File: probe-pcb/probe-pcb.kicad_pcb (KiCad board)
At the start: 2 copper layers, 38.8 x 48.2 mm, 36 parts, among them J1 IDC_HEADER_02x08, J2 IDC_HEADER_2x12, U1 SN74AXC8T245, U2 DS90LV047A, U3 MIC5205-3.3YM5, U4 DS90LV047A

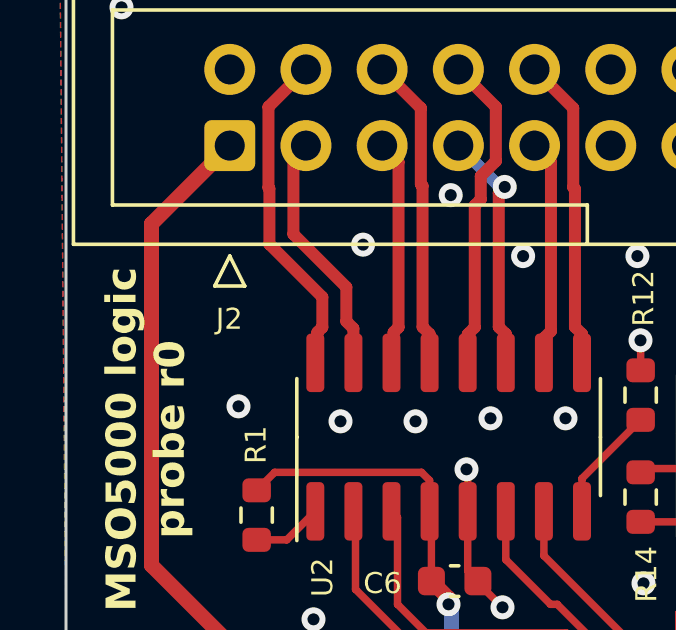
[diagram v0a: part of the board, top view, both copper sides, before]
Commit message: Add 3d model for 2x12 pin header (missing in kicad library), add readme
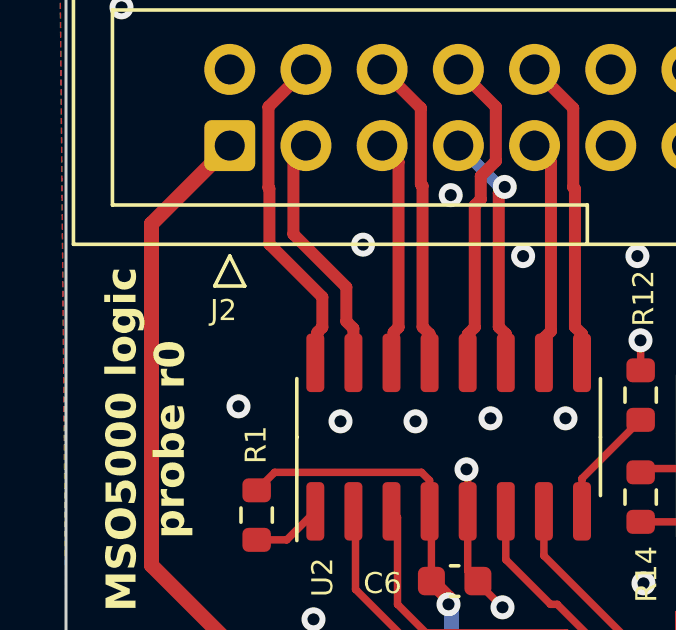
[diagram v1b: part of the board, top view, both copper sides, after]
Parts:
- J2: footprint Connector_IDC:IDC-Header_2x12_P2.54mm_Vertical -> idc:IDC-Header_2x12_P2.54mm_Vertical
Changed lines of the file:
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@@
     )
   )
-  (footprint "Connector_IDC:IDC-Header_2x12_P2.54mm_Vertical" (layer "F.Cu")
+  (footprint "idc:IDC-Header_2x12_P2.54mm_Vertical" (layer "F.Cu")
     (at 99.458 60.259 90)
     (descr "Through hole IDC box header, 2x12, 2.54mm pitch, DIN 41651 / IEC 60603-13, double rows, https://docs.google.com/spreadsheets/d/16SsEcesNF15N3Lb4niX7dcUr-NY5_MFPQhobNuNppn4/edit#gid=0")
@@
     (property "ki_keywords" "connector")
     (attr through_hole)
-    (fp_text reference "J2" (at -5.781 -0.017 180) (layer "F.SilkS")
+    (fp_text reference "J2" (at -5.491 -0.208) (layer "F.SilkS")
         (effects (font (size 0.7 0.7) (thickness 0.15)))
     )
@@
         (effects (font (size 1 1) (thickness 0.15)))
     )
-    (fp_text user "${REFERENCE}" (at 1.27 13.97) (layer "F.Fab")
+    (fp_text user "${REFERENCE}" (at 1.27 13.97 180) (layer "F.Fab")
         (effects (font (size 1 1) (thickness 0.15)))
     )
@@
     (pad "24" thru_hole circle (at 2.54 27.94 90) (size 1.7 1.7) (drill 1) (layers "*.Cu" "*.Mask")
       (net 2 "GND") (pinfunction "Pin_24") (pintype "passive"))
-    (model "${KICAD6_3DMODEL_DIR}/Connector_IDC.3dshapes/IDC-Header_2x12_P2.54mm_Vertical.wrl"
-      (offset (xyz 0 0 0))
+    (model "${KIPRJMOD}/../idc.pretty/IDC_2x12.STEP"
+      (offset (xyz -3 5 0))
       (scale (xyz 1 1 1))
-      (rotate (xyz 0 0 0))
+      (rotate (xyz -90 0 90))
     )
   )

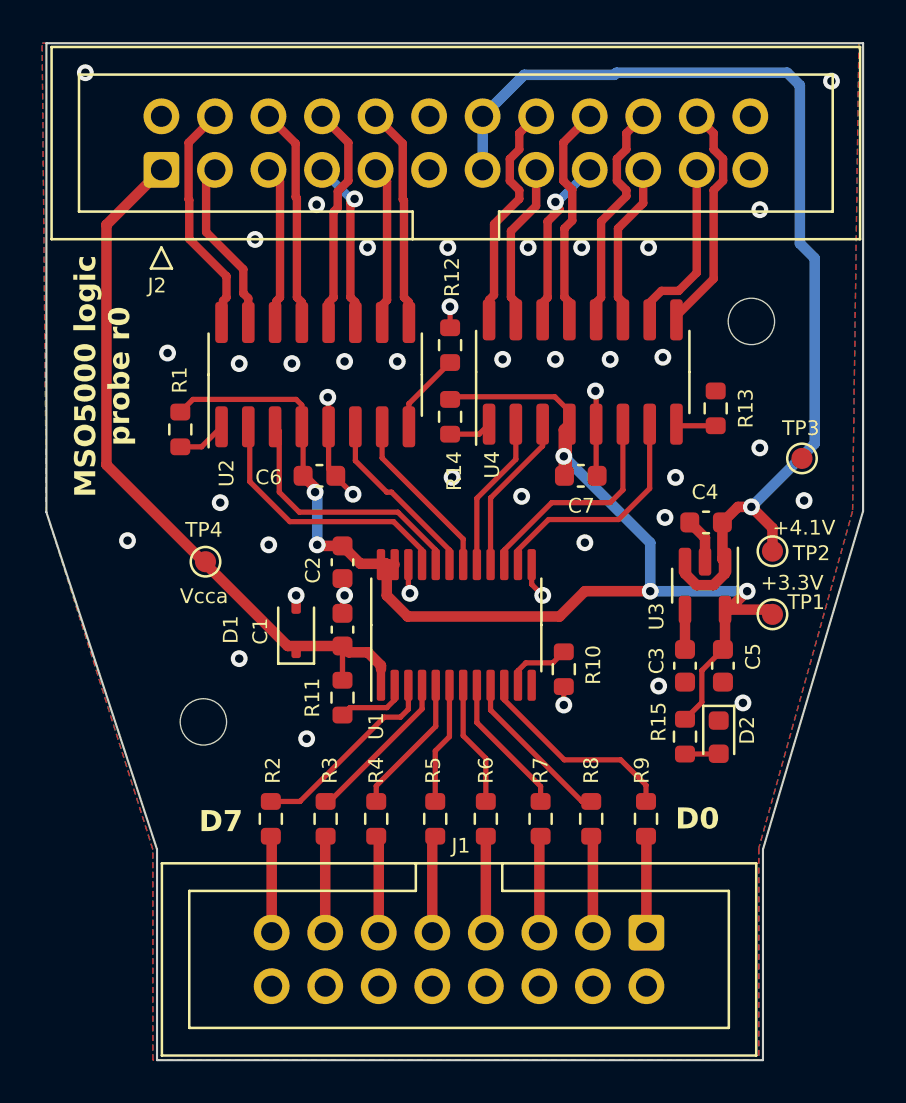
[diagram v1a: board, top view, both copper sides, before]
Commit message: Change zener diodes to 3.9V (should protect both 3.3V and 5V level shifters)
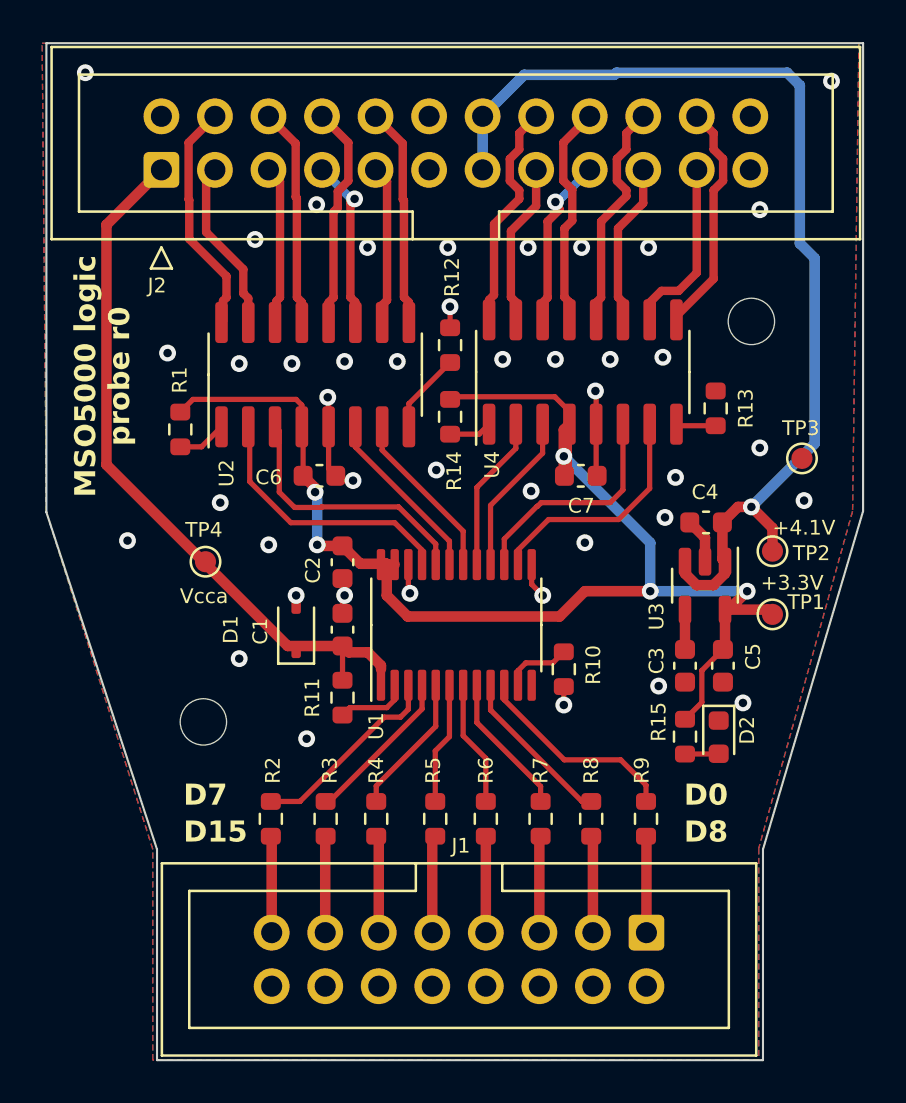
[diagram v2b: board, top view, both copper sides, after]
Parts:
- D1: value 3.6V 2% -> 3.9V 5%
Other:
- board text added: "D15"
- board text added: "D8"
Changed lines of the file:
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@@
     (descr "SOD-323")
     (tags "SOD-323")
-    (property "LCSC#" "C116949")
-    (property "MPN" "MM3Z3V6T1G")
-    (property "Manufacturer" "onsemi")
+    (property "LCSC#" "C5359777")
+    (property "MPN" "MM3Z3V9")
+    (property "Manufacturer" "Fosan")
     (property "Sheetfile" "probe-pcb.kicad_sch")
     (property "Sheetname" "")
@@
         (effects (font (size 0.7 0.7) (thickness 0.15)))
     )
-    (fp_text value "3.6V 2%" (at 0.1 1.9 90) (layer "F.Fab")
+    (fp_text value "3.9V 5%" (at 0.1 1.9 90) (layer "F.Fab")
         (effects (font (size 1 1) (thickness 0.15)))
     )
@@
   (gr_line (start 94 76.5) (end 99.25 92.5)
     (stroke (width 0.1) (type default)) (layer "Edge.Cuts"))
-  (gr_text "D0" (at 123.842 91.628) (layer "F.SilkS")
+  (gr_text "D0" (at 124.25 90.5) (layer "F.SilkS")
     (effects (font (size 1 1) (thickness 0.25) bold) (justify left bottom))
   )
-  (gr_text "D7" (at 101.236 91.755) (layer "F.SilkS")
+  (gr_text "D7" (at 100.5 90.5) (layer "F.SilkS")
+    (effects (font (size 1 1) (thickness 0.25) bold) (justify left bottom))
+  )
+  (gr_text "D15" (at 100.5 92.25) (layer "F.SilkS")
+    (effects (font (size 1 1) (thickness 0.25) bold) (justify left bottom))
+  )
+  (gr_text "D8" (at 124.25 92.25) (layer "F.SilkS")
     (effects (font (size 1 1) (thickness 0.25) bold) (justify left bottom))
   )
@@
   (segment (start 108.05 79.65) (end 108.05 80.35) (width 0.25) (layer "F.Cu") (net 2))
   (segment (start 107.39 74.435) (end 107.73 74.775) (width 0.25) (layer "F.Cu") (net 2))
+  (segment (start 108.55 75) (end 107.955 75) (width 0.25) (layer "F.Cu") (net 2))
   (segment (start 117.025 78.9875) (end 117.025 79.925) (width 0.25) (layer "F.Cu") (net 2))
   (segment (start 113.155 66.755) (end 113.15 66.75) (width 0.25) (layer "F.Cu") (net 2))
@@
   (segment (start 125.25 78.85) (end 125.25 77.7125) (width 0.5) (layer "F.Cu") (net 2))
   (segment (start 107.39 72.45) (end 107.39 71.09) (width 0.25) (layer "F.Cu") (net 2))
-  (segment (start 107.73 74.775) (end 107.73 74.83) (width 0.25) (layer "F.Cu") (net 2))
-  (segment (start 107.73 74.83) (end 108.55 75.65) (width 0.25) (layer "F.Cu") (net 2))
+  (segment (start 107.955 75) (end 107.73 74.775) (width 0.25) (layer "F.Cu") (net 2))
   (segment (start 111.175 80.275) (end 111.25 80.35) (width 0.25) (layer "F.Cu") (net 2))
   (via (at 119.55 77.95) (size 0.8) (drill 0.4) (layers "F.Cu" "B.Cu") (free) (net 2))
@@
   (via (at 123.85 74.85) (size 0.8) (drill 0.4) (layers "F.Cu" "B.Cu") (free) (net 2))
   (via (at 127.05 85.55) (size 0.8) (drill 0.4) (layers "F.Cu" "B.Cu") (free) (net 2))
-  (via (at 108.55 75.65) (size 0.8) (drill 0.4) (layers "F.Cu" "B.Cu") (net 2))
+  (via (at 108.55 75) (size 0.8) (drill 0.4) (layers "F.Cu" "B.Cu") (net 2))
   (via (at 119.397 63.942) (size 0.8) (drill 0.4) (layers "F.Cu" "B.Cu") (free) (net 2))
   (via (at 118.15 69.25) (size 0.8) (drill 0.4) (layers "F.Cu" "B.Cu") (free) (net 2))
@@
   (via (at 113.047 63.942) (size 0.8) (drill 0.4) (layers "F.Cu" "B.Cu") (free) (net 2))
   (via (at 105.65 69.45) (size 0.8) (drill 0.4) (layers "F.Cu" "B.Cu") (free) (net 2))
-  (via (at 113.25 74.85) (size 0.8) (drill 0.4) (layers "F.Cu" "B.Cu") (free) (net 2))
-  (via (at 116.55 75.75) (size 0.8) (drill 0.4) (layers "F.Cu" "B.Cu") (free) (net 2))
+  (via (at 112.5 74.5) (size 0.8) (drill 0.4) (layers "F.Cu" "B.Cu") (free) (net 2))
+  (via (at 117 75.5) (size 0.8) (drill 0.4) (layers "F.Cu" "B.Cu") (free) (net 2))
   (via (at 110.65 69.35) (size 0.8) (drill 0.4) (layers "F.Cu" "B.Cu") (free) (net 2))
   (via (at 120.75 69.25) (size 0.8) (drill 0.4) (layers "F.Cu" "B.Cu") (free) (net 2))
@@
   (segment (start 121.15 76.85) (end 122.625 75.375) (width 0.25) (layer "F.Cu") (net 44))
   (segment (start 117.823959 76.85) (end 121.15 76.85) (width 0.25) (layer "F.Cu") (net 44))
-  (segment (start 115.725 78.298959) (end 117.973959 76.05) (width 0.25) (layer "F.Cu") (net 45))
+  (segment (start 115.725 78.9875) (end 115.725 77.775) (width 0.25) (layer "F.Cu") (net 45))
+  (segment (start 115.725 77.775) (end 117.275 76.225) (width 0.25) (layer "F.Cu") (net 45))
+  (segment (start 117.475305 76.05) (end 120.75 76.05) (width 0.25) (layer "F.Cu") (net 45))
   (segment (start 121.355 75.445) (end 121.355 72.325) (width 0.25) (layer "F.Cu") (net 45))
-  (segment (start 115.725 78.9875) (end 115.725 78.298959) (width 0.25) (layer "F.Cu") (net 45))
-  (segment (start 117.973959 76.05) (end 120.75 76.05) (width 0.25) (layer "F.Cu") (net 45))
+  (segment (start 117.300305 76.225) (end 117.475305 76.05) (width 0.25) (layer "F.Cu") (net 45))
+  (segment (start 117.275 76.225) (end 117.300305 76.225) (width 0.25) (layer "F.Cu") (net 45))
   (segment (start 120.75 76.05) (end 121.355 75.445) (width 0.25) (layer "F.Cu") (net 45))
-  (segment (start 115.075 78.9875) (end 115.075 75.828147) (width 0.25) (layer "F.Cu") (net 46))
-  (segment (start 117.545 73.358147) (end 117.545 72.325) (width 0.25) (layer "F.Cu") (net 46))
-  (segment (start 115.075 75.828147) (end 117.545 73.358147) (width 0.25) (layer "F.Cu") (net 46))
-  (segment (start 116.275 73.991751) (end 116.275 72.325) (width 0.25) (layer "F.Cu") (net 47))
-  (segment (start 114.425 78.9875) (end 114.425 75.841751) (width 0.25) (layer "F.Cu") (net 47))
-  (segment (start 114.425 75.841751) (end 116.275 73.991751) (width 0.25) (layer "F.Cu") (net 47))
-  (segment (start 113.775 78.9875) (end 113.775 77.775) (width 0.25) (layer "F.Cu") (net 48))
-  (segment (start 109.93 73.93) (end 109.93 72.45) (width 0.25) (layer "F.Cu") (net 48))
-  (segment (start 113.775 77.775) (end 109.93 73.93) (width 0.25) (layer "F.Cu") (net 48))
-  (segment (start 113.125 78.298959) (end 110.376041 75.55) (width 0.25) (layer "F.Cu") (net 49))
-  (segment (start 110.15 75.55) (end 108.66 74.06) (width 0.25) (layer "F.Cu") (net 49))
-  (segment (start 113.125 78.9875) (end 113.125 78.298959) (width 0.25) (layer "F.Cu") (net 49))
-  (segment (start 108.66 74.06) (end 108.66 72.45) (width 0.25) (layer "F.Cu") (net 49))
-  (segment (start 110.376041 75.55) (end 110.15 75.55) (width 0.25) (layer "F.Cu") (net 49))
-  (segment (start 112.475 78.298959) (end 110.676041 76.5) (width 0.25) (layer "F.Cu") (net 50))
-  (segment (start 112.475 78.9875) (end 112.475 78.298959) (width 0.25) (layer "F.Cu") (net 50))
-  (segment (start 110.676041 76.5) (end 106 76.5) (width 0.25) (layer "F.Cu") (net 50))
-  (segment (start 106 76.5) (end 105.05 75.55) (width 0.25) (layer "F.Cu") (net 50))
+  (segment (start 115.075 78.9875) (end 115.075 76.175) (width 0.25) (layer "F.Cu") (net 46))
+  (segment (start 115.075 76.175) (end 117.545 73.705) (width 0.25) (layer "F.Cu") (net 46))
+  (segment (start 117.545 73.705) (end 117.545 72.325) (width 0.25) (layer "F.Cu") (net 46))
+  (segment (start 114.425 75.325) (end 116.275 73.475) (width 0.25) (layer "F.Cu") (net 47))
+  (segment (start 116.275 73.475) (end 116.275 72.325) (width 0.25) (layer "F.Cu") (net 47))
+  (segment (start 114.425 78.9875) (end 114.425 75.325) (width 0.25) (layer "F.Cu") (net 47))
+  (segment (start 113.775 77.4) (end 109.93 73.555) (width 0.25) (layer "F.Cu") (net 48))
+  (segment (start 109.93 73.555) (end 109.93 72.45) (width 0.25) (layer "F.Cu") (net 48))
+  (segment (start 113.775 78.9875) (end 113.775 77.4) (width 0.25) (layer "F.Cu") (net 48))
+  (segment (start 113.125 77.875) (end 108.66 73.41) (width 0.25) (layer "F.Cu") (net 49))
+  (segment (start 113.125 78.9875) (end 113.125 77.875) (width 0.25) (layer "F.Cu") (net 49))
+  (segment (start 108.66 73.41) (end 108.66 72.45) (width 0.25) (layer "F.Cu") (net 49))
+  (segment (start 112.475 78.01198) (end 110.71302 76.25) (width 0.25) (layer "F.Cu") (net 50))
   (segment (start 105.05 75.55) (end 105.05 72.65) (width 0.25) (layer "F.Cu") (net 50))
+  (segment (start 105.775 76.275) (end 105.05 75.55) (width 0.25) (layer "F.Cu") (net 50))
+  (segment (start 112.475 78.9875) (end 112.475 78.01198) (width 0.25) (layer "F.Cu") (net 50))
   (segment (start 105.05 72.65) (end 104.85 72.45) (width 0.25) (layer "F.Cu") (net 50))
-  (segment (start 111.825 78.298959) (end 110.476041 76.95) (width 0.25) (layer "F.Cu") (net 51))
+  (segment (start 107.075305 76.25) (end 107.050305 76.275) (width 0.25) (layer "F.Cu") (net 50))
+  (segment (start 110.71302 76.25) (end 107.075305 76.25) (width 0.25) (layer "F.Cu") (net 50))
+  (segment (start 107.050305 76.275) (end 105.775 76.275) (width 0.25) (layer "F.Cu") (net 50))
   (segment (start 103.65 72.52) (end 103.58 72.45) (width 0.25) (layer "F.Cu") (net 51))
-  (segment (start 110.476041 76.95) (end 105.55 76.95) (width 0.25) (layer "F.Cu") (net 51))
+  (segment (start 111.825 78.9875) (end 111.825 78.298959) (width 0.25) (layer "F.Cu") (net 51))
+  (segment (start 105.6 77) (end 103.65 75.05) (width 0.25) (layer "F.Cu") (net 51))
   (segment (start 103.65 75.05) (end 103.65 72.52) (width 0.25) (layer "F.Cu") (net 51))
-  (segment (start 105.55 76.95) (end 103.65 75.05) (width 0.25) (layer "F.Cu") (net 51))
-  (segment (start 111.825 78.9875) (end 111.825 78.298959) (width 0.25) (layer "F.Cu") (net 51))
+  (segment (start 110.526041 77) (end 105.6 77) (width 0.25) (layer "F.Cu") (net 51))
+  (segment (start 111.825 78.298959) (end 110.526041 77) (width 0.25) (layer "F.Cu") (net 51))
   (segment (start 125.8875 87.975) (end 125.9 87.9625) (width 0.25) (layer "F.Cu") (net 52))
   (segment (start 124.3 87.975) (end 125.8875 87.975) (width 0.25) (layer "F.Cu") (net 52))
